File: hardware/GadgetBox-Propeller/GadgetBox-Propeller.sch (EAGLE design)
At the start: 11 parts, among them IC1 P8X32A-Q44

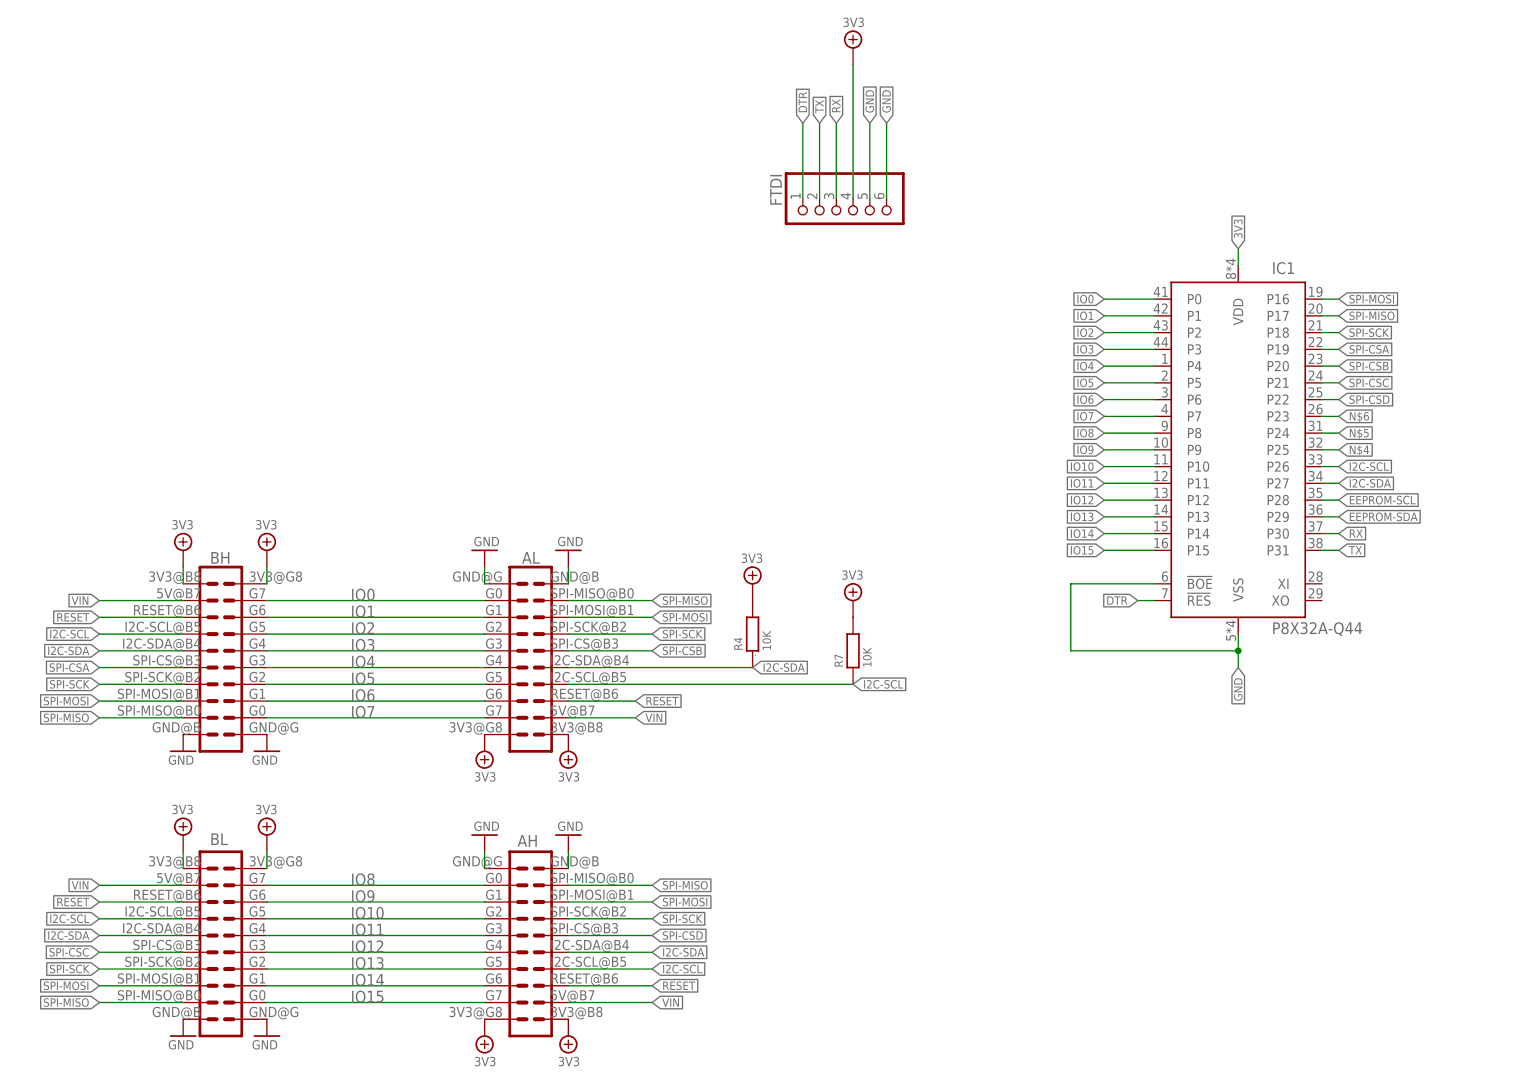
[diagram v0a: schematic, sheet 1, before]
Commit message: mostly done routing
added EEPROM and most routing
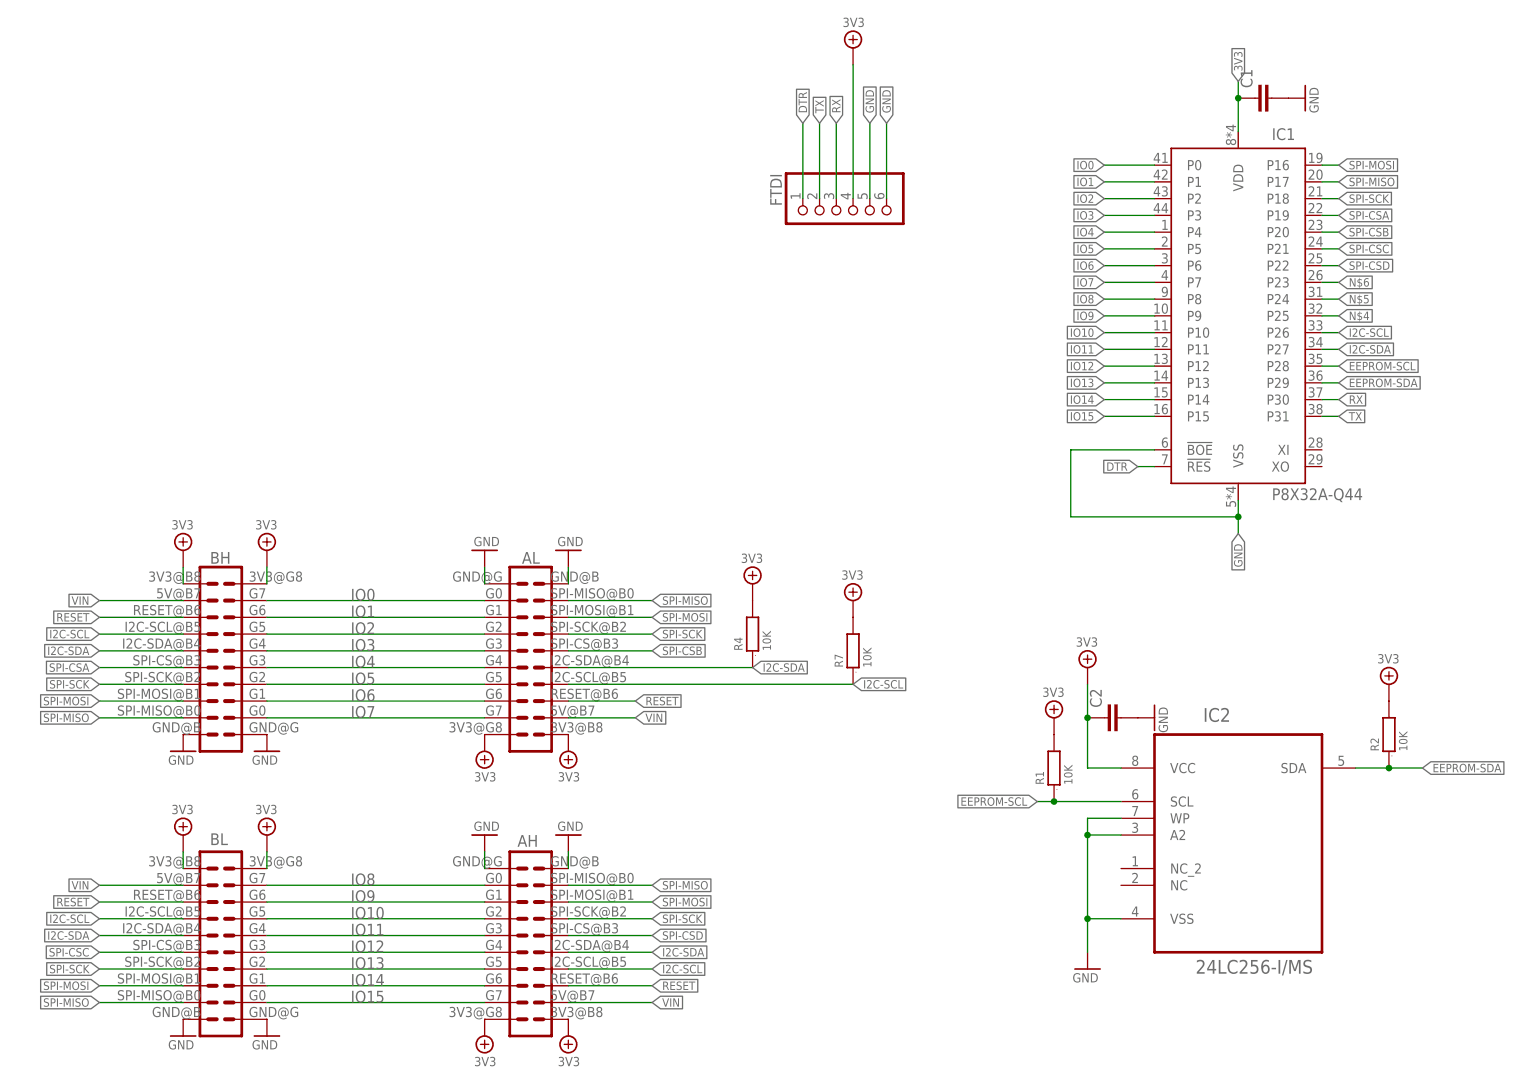
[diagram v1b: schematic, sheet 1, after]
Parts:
- added C1, C2: (no value), SparkFun-Passives:CAP0805
- added IC2: 24LC256-I/MS, Microchip_By_element14_Batch_1:24LC256-I/MS
- added R1, R2: 10K, GadgetFactory:R0603
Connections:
- net 3V3: now also C1.1, C2.1, IC2.VCC, R1A.2, R2A.2
- net EEPROM-SCL: now also IC2.SCL, R1A.1
- net EEPROM-SDA: now also IC2.SDA, R2A.1
- net GND: now also C1.2, C2.2, IC2.A2, IC2.VSS, IC2.WP
- net IO0: now also AL.G0
- net IO1: now also AL.G1
- net IO2: now also AL.G2
- net IO3: now also AL.G3
- net IO4: now also AL.G4
- net IO5: now also AL.G5
- net IO6: now also AL.G6
- net IO7: now also AL.G7
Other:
- moved on the sheet: IC1

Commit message: Propeller mostly done
Need to validate FTDI connection and do eCog graphics
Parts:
- added Q1: (no value), adafruit:CRYSTALSM49
- added Q3: (no value), adafruit:CRYSTALHC49U-V
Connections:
- removed net DTR: FTDI.1
- removed net N$1: IC1.!RES
- new net N$2: IC1.XI, Q1.1, Q3.1
- new net N$3: IC1.XO, Q1.2, Q3.2
- net RESET: now also FTDI.1, IC1.!RES
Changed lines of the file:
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@@
 <part name="GND3" library="GadgetFactory" deviceset="GND" device=""/>
 <part name="GND4" library="GadgetFactory" deviceset="GND" device=""/>
+<part name="Q1" library="adafruit" deviceset="CRYSTAL" device="SM49"/>
+<part name="Q3" library="adafruit" deviceset="CRYSTAL" device="HC49U-V"/>
 </parts>
 <sheets>
@@
 <instance part="GND3" gate="A" x="190.5" y="66.04" rot="R90"/>
 <instance part="GND4" gate="A" x="213.36" y="160.02" rot="R90"/>
+<instance part="Q1" gate="G$1" x="223.52" y="104.14" rot="R270"/>
+<instance part="Q3" gate="G$1" x="233.68" y="104.14" rot="R270"/>
 </instances>
 <busses>
@@
 <wire x1="101.6" y1="68.58" x2="111.76" y2="68.58" width="0.2032" layer="91"/>
 <label x="111.76" y="68.58" size="1.27" layer="95" xref="yes"/>
+</segment>
+<segment>
+<pinref part="FTDI" gate="A" pin="1"/>
+<wire x1="137.16" y1="144.78" x2="137.16" y2="156.21" width="0.2032" layer="91"/>
+<label x="137.16" y="156.21" size="1.27" layer="95" rot="MR90" xref="yes"/>
+</segment>
+<segment>
+<pinref part="IC1" gate="G$1" pin="!RES"/>
+<wire x1="190.5" y1="104.14" x2="187.96" y2="104.14" width="0.1524" layer="91"/>
+<label x="187.96" y="104.14" size="1.27" layer="95" rot="R180" xref="yes"/>
 </segment>
 </net>
@@
 </segment>
 </net>
-<net name="DTR" class="0">
-<segment>
-<pinref part="FTDI" gate="A" pin="1"/>
-<wire x1="137.16" y1="144.78" x2="137.16" y2="156.21" width="0.2032" layer="91"/>
-<label x="137.16" y="156.21" size="1.27" layer="95" rot="MR90" xref="yes"/>
-<label x="187.96" y="104.14" size="1.27" layer="95" rot="MR0" xref="yes"/>
-</segment>
-</net>
 <net name="VIN" class="0">
 <segment>
@@
 <label x="218.44" y="111.76" size="1.27" layer="95" rot="MR180" xref="yes"/>
 <pinref part="IC1" gate="G$1" pin="P31"/>
-</segment>
-</net>
-<net name="N$1" class="0">
-<segment>
-<pinref part="IC1" gate="G$1" pin="!RES"/>
-<wire x1="190.5" y1="104.14" x2="187.96" y2="104.14" width="0.1524" layer="91"/>
 </segment>
 </net>
@@
 </segment>
 </net>
+<net name="N$2" class="0">
+<segment>
+<pinref part="IC1" gate="G$1" pin="XI"/>
+<pinref part="Q3" gate="G$1" pin="1"/>
+<wire x1="215.9" y1="106.68" x2="223.52" y2="106.68" width="0.1524" layer="91"/>
+<pinref part="Q1" gate="G$1" pin="1"/>
+<junction x="223.52" y="106.68"/>
+<wire x1="223.52" y1="106.68" x2="233.68" y2="106.68" width="0.1524" layer="91"/>
+</segment>
+</net>
+<net name="N$3" class="0">
+<segment>
+<pinref part="Q3" gate="G$1" pin="2"/>
+<pinref part="Q1" gate="G$1" pin="2"/>
+<wire x1="233.68" y1="101.6" x2="223.52" y2="101.6" width="0.1524" layer="91"/>
+<wire x1="223.52" y1="101.6" x2="218.44" y2="101.6" width="0.1524" layer="91"/>
+<wire x1="218.44" y1="101.6" x2="218.44" y2="104.14" width="0.1524" layer="91"/>
+<pinref part="IC1" gate="G$1" pin="XO"/>
+<wire x1="218.44" y1="104.14" x2="215.9" y2="104.14" width="0.1524" layer="91"/>
+<junction x="223.52" y="101.6"/>
+</segment>
+</net>
